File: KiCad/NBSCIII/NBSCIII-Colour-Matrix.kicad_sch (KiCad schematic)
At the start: 24 parts, among them U9 LM324

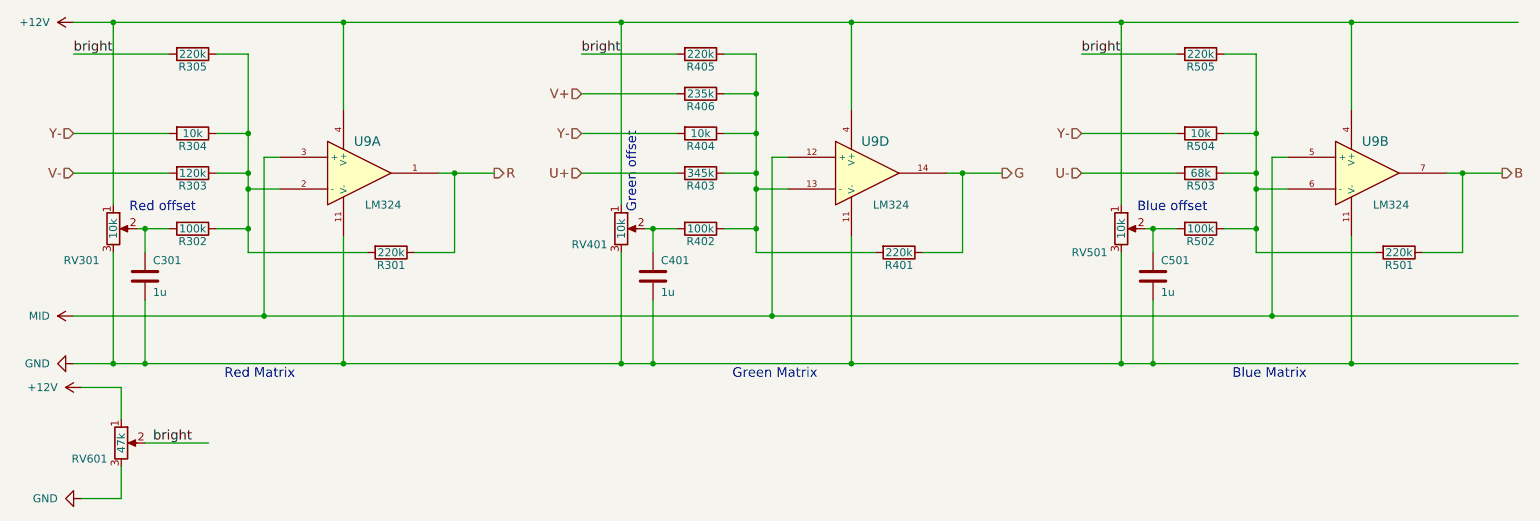
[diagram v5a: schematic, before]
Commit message: derescue lm324
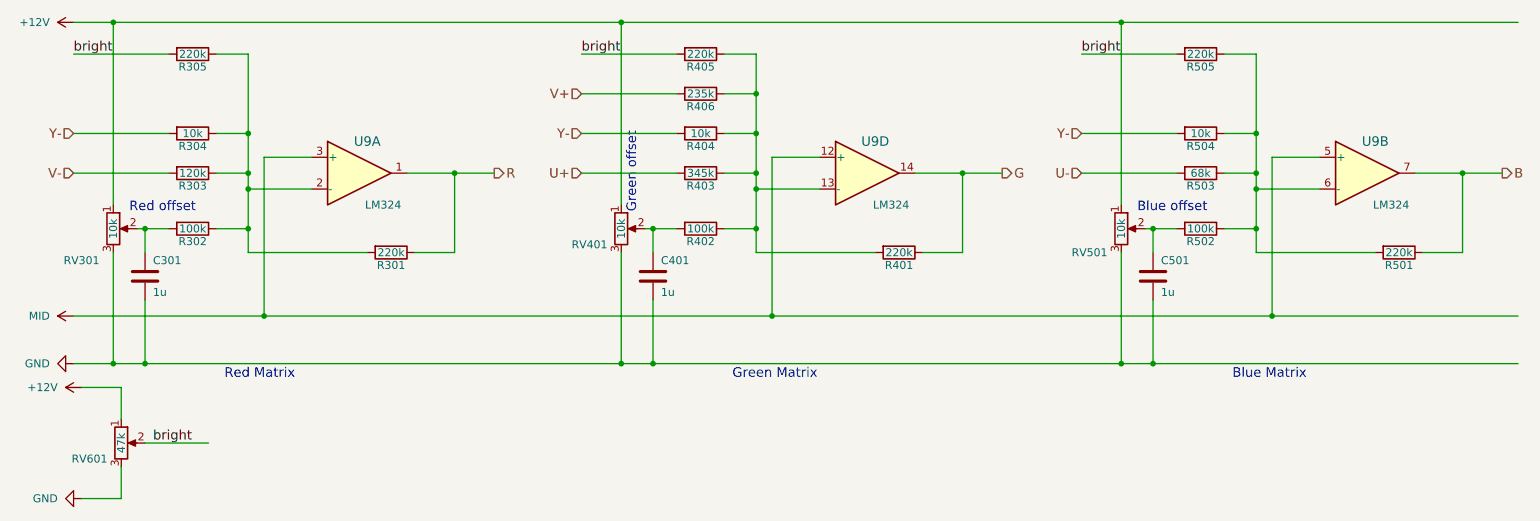
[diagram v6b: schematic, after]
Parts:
- U9: symbol NBSCIII-rescue:LM324 -> Amplifier_Operational:LM324
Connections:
- net +12V: no longer U9.4 (V+), U9.4 (V+), U9.4 (V+)
- net GND: no longer U9.11 (V-), U9.11 (V-), U9.11 (V-)
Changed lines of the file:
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@@
   (junction (at 219.71 69.85) (diameter 0) (color 0 0 0 0)
   )
-  (junction (at 154.94 91.44) (diameter 0) (color 0 0 0 0)
-  )
   (junction (at 91.44 60.96) (diameter 0) (color 0 0 0 0)
   )
-  (junction (at 73.66 36.83) (diameter 0) (color 0 0 0 0)
-  )
   (junction (at 60.96 83.82) (diameter 0) (color 0 0 0 0)
   )
@@
   (junction (at 123.19 69.85) (diameter 0) (color 0 0 0 0)
   )
-  (junction (at 154.94 36.83) (diameter 0) (color 0 0 0 0)
-  )
   (junction (at 41.91 69.85) (diameter 0) (color 0 0 0 0)
   )
@@
   (junction (at 41.91 91.44) (diameter 0) (color 0 0 0 0)
   )
-  (junction (at 73.66 91.44) (diameter 0) (color 0 0 0 0)
-  )
   (junction (at 198.12 91.44) (diameter 0) (color 0 0 0 0)
   )
@@
   (junction (at 219.71 60.96) (diameter 0) (color 0 0 0 0)
   )
-  (junction (at 234.95 91.44) (diameter 0) (color 0 0 0 0)
-  )
   (junction (at 203.2 91.44) (diameter 0) (color 0 0 0 0)
   )
@@
   (junction (at 139.7 48.26) (diameter 0) (color 0 0 0 0)
   )
-  (junction (at 234.95 36.83) (diameter 0) (color 0 0 0 0)
-  )
   (junction (at 123.19 91.44) (diameter 0) (color 0 0 0 0)
   )
@@
     (stroke (width 0) (type default) (color 0 0 0 0))
   )
-  (wire (pts (xy 234.95 91.44) (xy 203.2 91.44))
-    (stroke (width 0) (type default) (color 0 0 0 0))
-  )
   (wire (pts (xy 36.83 91.44) (xy 30.48 91.44))
     (stroke (width 0) (type default) (color 0 0 0 0))
@@
     (stroke (width 0) (type default) (color 0 0 0 0))
   )
-  (wire (pts (xy 144.78 58.42) (xy 142.24 58.42))
+  (wire (pts (xy 142.24 58.42) (xy 149.86 58.42))
     (stroke (width 0) (type default) (color 0 0 0 0))
   )
@@
     (stroke (width 0) (type default) (color 0 0 0 0))
   )
-  (wire (pts (xy 73.66 91.44) (xy 41.91 91.44))
+  (wire (pts (xy 41.91 91.44) (xy 118.11 91.44))
     (stroke (width 0) (type default) (color 0 0 0 0))
   )
@@
     (stroke (width 0) (type default) (color 0 0 0 0))
   )
-  (wire (pts (xy 118.11 36.83) (xy 73.66 36.83))
-    (stroke (width 0) (type default) (color 0 0 0 0))
-  )
   (wire (pts (xy 30.48 54.61) (xy 45.72 54.61))
     (stroke (width 0) (type default) (color 0 0 0 0))
@@
     (stroke (width 0) (type default) (color 0 0 0 0))
   )
-  (wire (pts (xy 234.95 71.12) (xy 234.95 91.44))
-    (stroke (width 0) (type default) (color 0 0 0 0))
-  )
   (wire (pts (xy 222.25 58.42) (xy 222.25 83.82))
     (stroke (width 0) (type default) (color 0 0 0 0))
   )
-  (wire (pts (xy 73.66 36.83) (xy 36.83 36.83))
+  (wire (pts (xy 36.83 36.83) (xy 118.11 36.83))
     (stroke (width 0) (type default) (color 0 0 0 0))
   )
@@
     (stroke (width 0) (type default) (color 0 0 0 0))
   )
-  (wire (pts (xy 154.94 36.83) (xy 118.11 36.83))
-    (stroke (width 0) (type default) (color 0 0 0 0))
-  )
   (wire (pts (xy 139.7 73.66) (xy 139.7 69.85))
     (stroke (width 0) (type default) (color 0 0 0 0))
   )
-  (wire (pts (xy 261.62 91.44) (xy 234.95 91.44))
-    (stroke (width 0) (type default) (color 0 0 0 0))
-  )
-  (wire (pts (xy 154.94 91.44) (xy 123.19 91.44))
+  (wire (pts (xy 203.2 91.44) (xy 261.62 91.44))
+    (stroke (width 0) (type default) (color 0 0 0 0))
+  )
+  (wire (pts (xy 123.19 91.44) (xy 198.12 91.44))
+    (stroke (width 0) (type default) (color 0 0 0 0))
+  )
+  (wire (pts (xy 60.96 58.42) (xy 68.58 58.42))
     (stroke (width 0) (type default) (color 0 0 0 0))
   )
@@
     (stroke (width 0) (type default) (color 0 0 0 0))
   )
-  (wire (pts (xy 198.12 91.44) (xy 154.94 91.44))
-    (stroke (width 0) (type default) (color 0 0 0 0))
-  )
   (wire (pts (xy 58.42 60.96) (xy 58.42 54.61))
     (stroke (width 0) (type default) (color 0 0 0 0))
@@
     (stroke (width 0) (type default) (color 0 0 0 0))
   )
-  (wire (pts (xy 224.79 58.42) (xy 222.25 58.42))
-    (stroke (width 0) (type default) (color 0 0 0 0))
-  )
-  (wire (pts (xy 91.44 60.96) (xy 88.9 60.96))
+  (wire (pts (xy 222.25 58.42) (xy 229.87 58.42))
+    (stroke (width 0) (type default) (color 0 0 0 0))
+  )
+  (wire (pts (xy 83.82 60.96) (xy 91.44 60.96))
     (stroke (width 0) (type default) (color 0 0 0 0))
   )
@@
     (stroke (width 0) (type default) (color 0 0 0 0))
   )
-  (wire (pts (xy 198.12 36.83) (xy 154.94 36.83))
+  (wire (pts (xy 118.11 36.83) (xy 198.12 36.83))
     (stroke (width 0) (type default) (color 0 0 0 0))
   )
@@
     (stroke (width 0) (type default) (color 0 0 0 0))
   )
-  (wire (pts (xy 73.66 50.8) (xy 73.66 36.83))
-    (stroke (width 0) (type default) (color 0 0 0 0))
-  )
   (wire (pts (xy 58.42 73.66) (xy 77.47 73.66))
     (stroke (width 0) (type default) (color 0 0 0 0))
   )
+  (wire (pts (xy 245.11 60.96) (xy 252.73 60.96))
+    (stroke (width 0) (type default) (color 0 0 0 0))
+  )
   (wire (pts (xy 139.7 54.61) (xy 139.7 48.26))
     (stroke (width 0) (type default) (color 0 0 0 0))
@@
     (stroke (width 0) (type default) (color 0 0 0 0))
   )
-  (wire (pts (xy 139.7 63.5) (xy 144.78 63.5))
-    (stroke (width 0) (type default) (color 0 0 0 0))
-  )
-  (wire (pts (xy 154.94 71.12) (xy 154.94 91.44))
-    (stroke (width 0) (type default) (color 0 0 0 0))
-  )
-  (wire (pts (xy 234.95 50.8) (xy 234.95 36.83))
+  (wire (pts (xy 139.7 63.5) (xy 149.86 63.5))
     (stroke (width 0) (type default) (color 0 0 0 0))
   )
@@
     (stroke (width 0) (type default) (color 0 0 0 0))
   )
-  (wire (pts (xy 73.66 71.12) (xy 73.66 91.44))
-    (stroke (width 0) (type default) (color 0 0 0 0))
-  )
   (wire (pts (xy 41.91 91.44) (xy 36.83 91.44))
     (stroke (width 0) (type default) (color 0 0 0 0))
@@
     (stroke (width 0) (type default) (color 0 0 0 0))
   )
-  (wire (pts (xy 261.62 36.83) (xy 234.95 36.83))
-    (stroke (width 0) (type default) (color 0 0 0 0))
-  )
-  (wire (pts (xy 252.73 60.96) (xy 250.19 60.96))
-    (stroke (width 0) (type default) (color 0 0 0 0))
-  )
   (wire (pts (xy 201.93 69.85) (xy 203.2 69.85))
     (stroke (width 0) (type default) (color 0 0 0 0))
@@
     (stroke (width 0) (type default) (color 0 0 0 0))
   )
-  (wire (pts (xy 234.95 36.83) (xy 198.12 36.83))
+  (wire (pts (xy 198.12 36.83) (xy 261.62 36.83))
     (stroke (width 0) (type default) (color 0 0 0 0))
   )
@@
     (stroke (width 0) (type default) (color 0 0 0 0))
   )
-  (wire (pts (xy 219.71 63.5) (xy 224.79 63.5))
+  (wire (pts (xy 219.71 63.5) (xy 229.87 63.5))
     (stroke (width 0) (type default) (color 0 0 0 0))
   )
@@
     (stroke (width 0) (type default) (color 0 0 0 0))
   )
-  (wire (pts (xy 63.5 58.42) (xy 60.96 58.42))
-    (stroke (width 0) (type default) (color 0 0 0 0))
-  )
   (wire (pts (xy 41.91 81.28) (xy 41.91 91.44))
     (stroke (width 0) (type default) (color 0 0 0 0))
@@
     (stroke (width 0) (type default) (color 0 0 0 0))
   )
-  (wire (pts (xy 154.94 50.8) (xy 154.94 36.83))
-    (stroke (width 0) (type default) (color 0 0 0 0))
-  )
   (wire (pts (xy 58.42 63.5) (xy 58.42 60.96))
     (stroke (width 0) (type default) (color 0 0 0 0))
@@
     (stroke (width 0) (type default) (color 0 0 0 0))
   )
-  (wire (pts (xy 58.42 63.5) (xy 63.5 63.5))
+  (wire (pts (xy 58.42 63.5) (xy 68.58 63.5))
     (stroke (width 0) (type default) (color 0 0 0 0))
   )
@@
     (stroke (width 0) (type default) (color 0 0 0 0))
   )
-  (wire (pts (xy 118.11 91.44) (xy 73.66 91.44))
-    (stroke (width 0) (type default) (color 0 0 0 0))
-  )
-  (wire (pts (xy 172.72 60.96) (xy 170.18 60.96))
+  (wire (pts (xy 165.1 60.96) (xy 172.72 60.96))
     (stroke (width 0) (type default) (color 0 0 0 0))
   )
@@
     (effects (font (size 1.524 1.524)) (justify right))
   )
-  (symbol (lib_id "NBSCIII-rescue:LM324") (at 76.2 60.96 0) (unit 1)
+  (symbol (lib_id "Amplifier_Operational:LM324") (at 76.2 60.96 0) (unit 1)
     (in_bom yes) (on_board yes)
     (property "Reference" "U9" (id 0) (at 77.47 55.88 0)
@@
       (effects (font (size 1.27 1.27)) hide)
     )
-    (pin "11")
-    (pin "4")
     (pin "1")
     (pin "2")
@@
     (pin "13")
     (pin "14")
+    (pin "11")
+    (pin "4")
   )
   (symbol (lib_id "Device:R") (at 81.28 73.66 270) (unit 1)
@@
     (pin "2")
   )
-  (symbol (lib_id "NBSCIII-rescue:LM324") (at 157.48 60.96 0) (unit 4)
+  (symbol (lib_id "Amplifier_Operational:LM324") (at 157.48 60.96 0) (unit 4)
     (in_bom yes) (on_board yes)
     (property "Reference" "U9" (id 0) (at 158.75 55.88 0)
@@
       (effects (font (size 1.27 1.27)) hide)
     )
-    (pin "11")
-    (pin "4")
     (pin "1")
     (pin "2")
@@
     (pin "13")
     (pin "14")
+    (pin "11")
+    (pin "4")
   )
   (symbol (lib_id "Device:R") (at 162.56 73.66 270) (unit 1)
@@
     (pin "2")
   )
-  (symbol (lib_id "NBSCIII-rescue:LM324") (at 237.49 60.96 0) (unit 2)
+  (symbol (lib_id "Amplifier_Operational:LM324") (at 237.49 60.96 0) (unit 2)
     (in_bom yes) (on_board yes)
     (property "Reference" "U9" (id 0) (at 238.76 55.88 0)
@@
       (effects (font (size 1.27 1.27)) hide)
     )
-    (pin "11")
-    (pin "4")
     (pin "1")
     (pin "2")
@@
     (pin "13")
     (pin "14")
+    (pin "11")
+    (pin "4")
   )
   (symbol (lib_id "Device:R") (at 242.57 73.66 270) (unit 1)
